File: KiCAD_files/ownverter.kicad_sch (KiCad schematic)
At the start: 10 parts, among them J101 Harting-15 and Wago 6

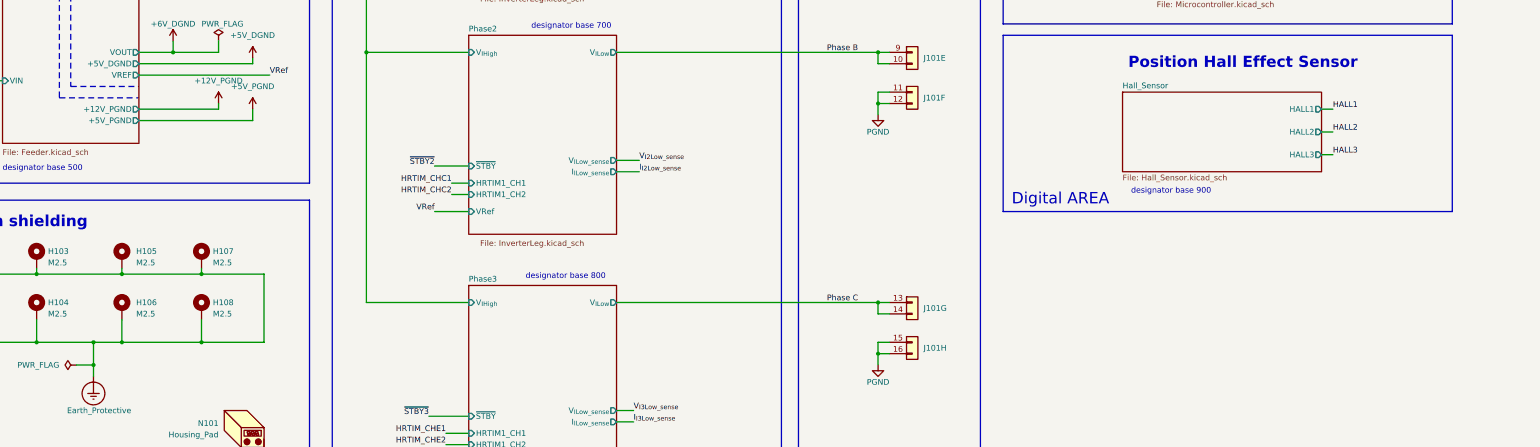
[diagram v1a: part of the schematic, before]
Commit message: better comments, especially for temp sens
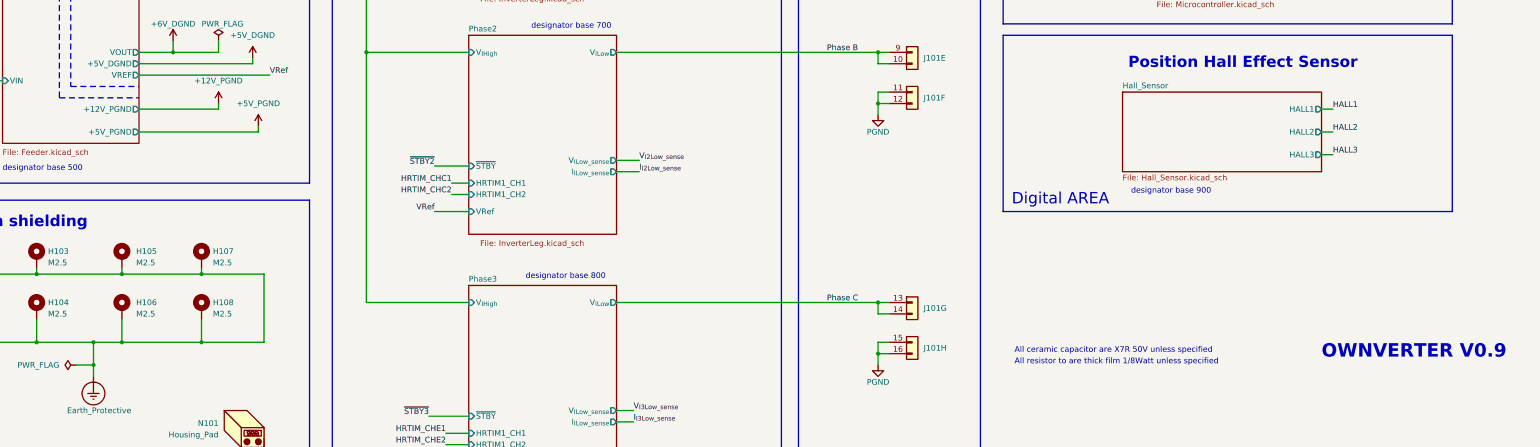
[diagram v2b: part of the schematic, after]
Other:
- note added: "All ceramic capacitor are X7R 50V unless specified"
- note added: "All resistor to are thick film 1/8Watt unless specified"
- note added: "OWNVERTER V0.9"
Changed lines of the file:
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@@
     (stroke (width 0) (type default))
   )
-  (wire (pts (xy 105.41 115.57) (xy 130.81 115.57))
+  (wire (pts (xy 105.41 118.11) (xy 132.08 118.11))
     (stroke (width 0) (type default))
   )
@@
     (stroke (width 0) (type default))
   )
-  (wire (pts (xy 130.81 113.03) (xy 130.81 115.57))
+  (wire (pts (xy 132.08 116.84) (xy 132.08 118.11))
     (stroke (width 0) (type default))
   )
@@
     (stroke (width 0) (type default))
     (fill (type none))
+  )
+  (text "All ceramic capacitor are X7R 50V unless specified"
+    (at 300.99 167.64 0)
+    (effects (font (size 1.27 1.27)) (justify left bottom))
   )
   (text "MCU\n" (at 342.9 33.02 0)
@@
   (text "Earth shielding" (at 64.77 139.7 0)
     (effects (font (face "Arial") (size 2.4892 2.4892) (thickness 0.4978) bold) (justify left bottom))
+  )
+  (text "OWNVERTER V0.9" (at 369.57 168.91 0)
+    (effects (font (size 3 3) (thickness 0.6) bold) (justify left bottom))
+  )
+  (text "All resistor to are thick film 1/8Watt unless specified"
+    (at 300.99 170.18 0)
+    (effects (font (size 1.27 1.27)) (justify left bottom))
   )
   (text "Position Hall Effect Sensor" (at 326.39 104.14 0)
@@
     )
   )
-  (symbol (lib_id "Symbols:+5V_PGND") (at 130.81 113.03 0) (unit 1)
+  (symbol (lib_id "Symbols:+5V_PGND") (at 132.08 116.84 0) (unit 1)
     (in_bom no) (on_board no) (dnp no)
-    (property "Reference" "#PWR0105" (at 132.588 113.03 90)
-      (effects (font (size 1.27 1.27)) hide)
-    )
-    (property "Value" "+5V_PGND" (at 130.81 107.95 0)
+    (property "Reference" "#PWR0105" (at 133.858 116.84 90)
+      (effects (font (size 1.27 1.27)) hide)
+    )
+    (property "Value" "+5V_PGND" (at 132.08 111.76 0)
       (effects (font (size 1.27 1.27)))
     )
-    (property "Footprint" "" (at 133.985 110.49 0)
-      (effects (font (size 1.27 1.27)) hide)
-    )
-    (property "Datasheet" "" (at 133.985 110.49 0)
+    (property "Footprint" "" (at 135.255 114.3 0)
+      (effects (font (size 1.27 1.27)) hide)
+    )
+    (property "Datasheet" "" (at 135.255 114.3 0)
       (effects (font (size 1.27 1.27)) hide)
     )
@@
       (effects (font (size 1.27 1.27)) (justify right))
     )
-    (pin "+5V_PGND" output (at 105.41 115.57 0)
-      (effects (font (size 1.27 1.27)) (justify right))
-    )
+    (pin "+5V_PGND" output (at 105.41 118.11 0)
+      (effects (font (size 1.27 1.27)) (justify right))
+    )

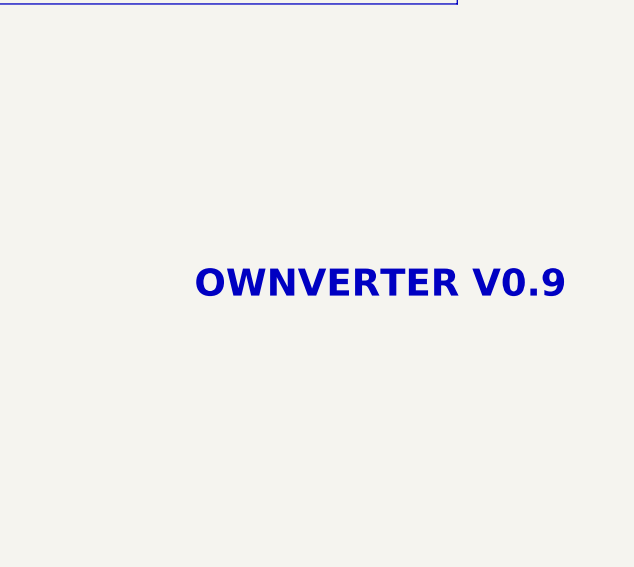
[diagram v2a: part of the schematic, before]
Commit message: Schematic freeze before PCB modifications
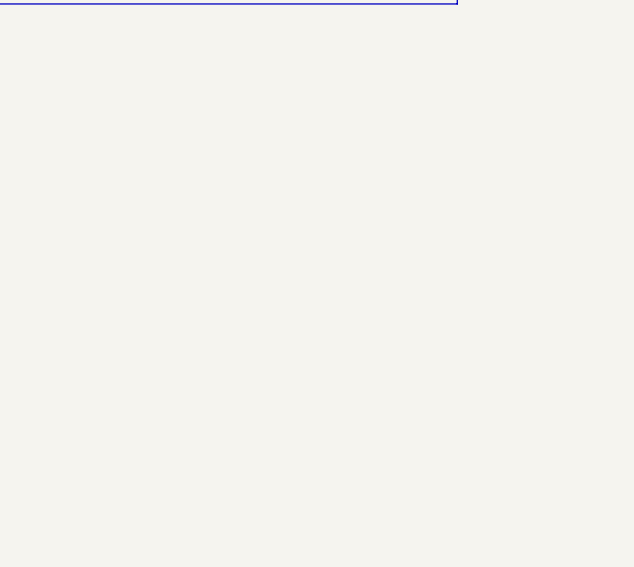
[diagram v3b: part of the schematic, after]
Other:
- note removed: "OWNVERTER V0.9"
- title: OWNVERTER V0.1 -> OWNVERTER V1.0
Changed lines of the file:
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@@
   (paper "A3")
   (title_block
-    (title "OWNVERTER V0.1")
+    (title "OWNVERTER V1.0")
     (comment 1 "TWR")
   )
@@
     (effects (font (face "Arial") (size 2.4892 2.4892) (thickness 0.4978) bold) (justify left bottom))
   )
-  (text "OWNVERTER V0.9" (at 369.57 168.91 0)
-    (effects (font (size 3 3) (thickness 0.6) bold) (justify left bottom))
-  )
   (text "All resistor to are thick film 1/8Watt unless specified"

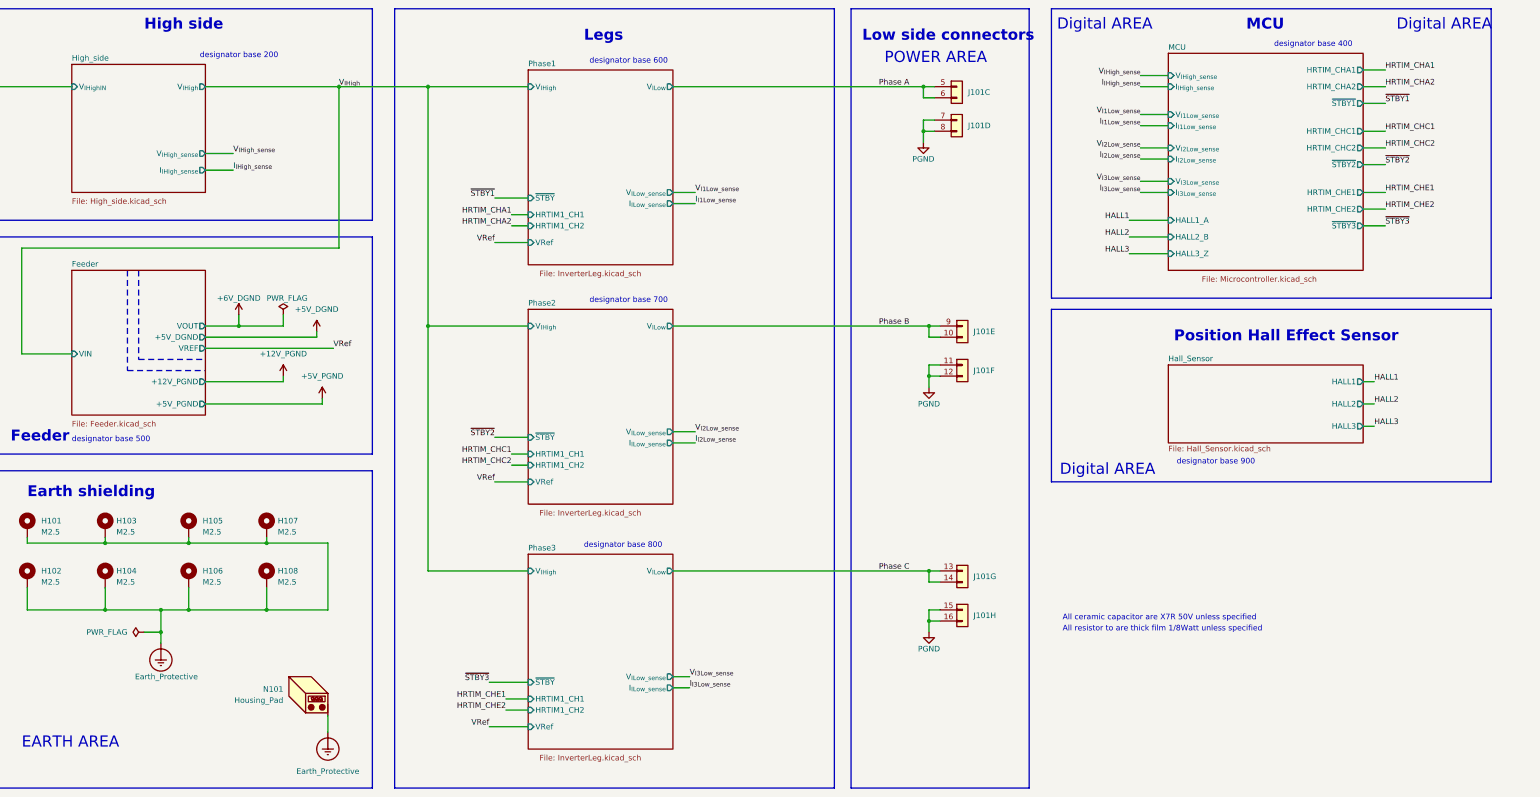
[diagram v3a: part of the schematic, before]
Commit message: changed schematic net labels for better comprehension
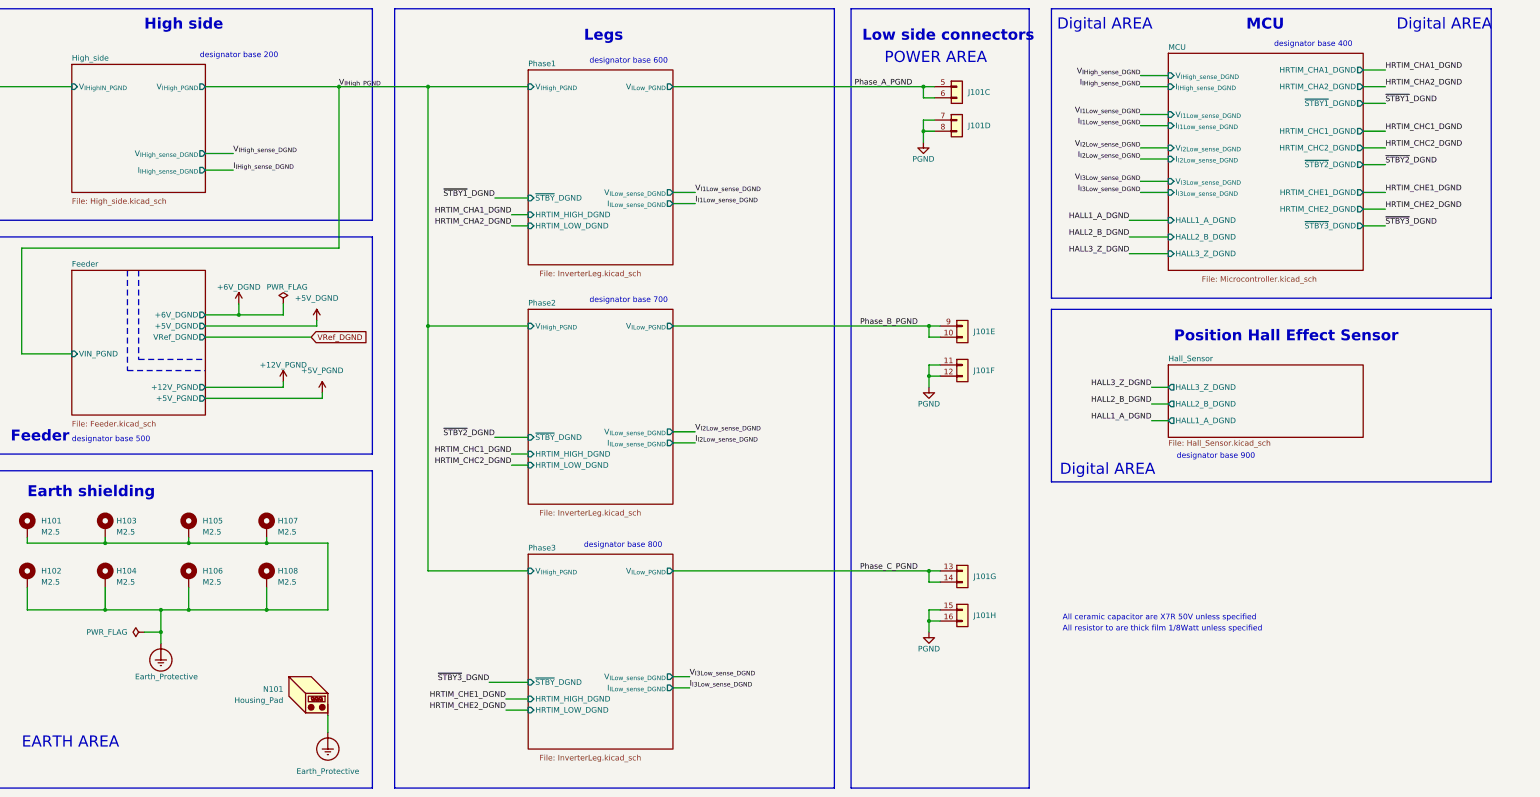
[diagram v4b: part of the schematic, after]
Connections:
- net High_side/V_{IHighIN} renamed High_side/V_{IHighIN_PGND}
- net Phase A renamed Phase_A_PGND
- net Phase B renamed Phase_B_PGND
- net Phase C renamed Phase_C_PGND
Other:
- sheet Feeder ports: added +6V_DGND, VIN_PGND, VRef_DGND; removed VIN, VOUT, VREF
- sheet Hall_Sensor ports: added HALL1_A_DGND, HALL2_B_DGND, HALL3_Z_DGND; removed HALL1, HALL2, HALL3
- sheet High_side ports: added I_{IHigh_sense_DGND}, V_{IHighIN_PGND}, V_{IHigh_PGND}, V_{IHigh_sense_DGND}; removed I_{IHigh_sense}, V_{IHighIN}, V_{IHigh_sense}, V_{IHigh}
- sheet MCU ports: added HALL1_A_DGND, HALL2_B_DGND, HALL3_Z_DGND, HRTIM_CHA1_DGND, HRTIM_CHA2_DGND, HRTIM_CHC1_DGND, HRTIM_CHC2_DGND, HRTIM_CHE1_DGND, HRTIM_CHE2_DGND, I_{I1Low_sense_DGND}, I_{I2Low_sense_DGND}, I_{I3Low_sense_DGND}, I_{IHigh_sense_DGND}, V_{I1Low_sense_DGND}, V_{I2Low_sense_DGND}, V_{I3Low_sense_DGND}, V_{IHigh_sense_DGND}, ~{STBY1}_DGND, ~{STBY2}_DGND, ~{STBY3}_DGND; removed HALL1_A, HALL2_B, HALL3_Z, HRTIM_CHA1, HRTIM_CHA2, HRTIM_CHC1, HRTIM_CHC2, HRTIM_CHE1, HRTIM_CHE2, I_{I1Low_sense}, I_{I2Low_sense}, I_{I3Low_sense}, I_{IHigh_sense}, V_{I1Low_sense}, V_{I2Low_sense}, V_{I3Low_sense}, V_{IHigh_sense}, ~{STBY1}, ~{STBY2}, ~{STBY3}
- sheet Phase1 ports: added HRTIM_HIGH_DGND, HRTIM_LOW_DGND, I_{ILow_sense_DGND}, V_{IHigh_PGND}, V_{ILow_PGND}, V_{ILow_sense_DGND}, ~{STBY}_DGND; removed HRTIM1_CH1, HRTIM1_CH2, I_{ILow_sense}, VRef, V_{IHigh}, V_{ILow_sense}, V_{ILow}, ~{STBY}
- sheet Phase2 ports: added HRTIM_HIGH_DGND, HRTIM_LOW_DGND, I_{ILow_sense_DGND}, V_{IHigh_PGND}, V_{ILow_PGND}, V_{ILow_sense_DGND}, ~{STBY}_DGND; removed HRTIM1_CH1, HRTIM1_CH2, I_{ILow_sense}, VRef, V_{IHigh}, V_{ILow_sense}, V_{ILow}, ~{STBY}
- sheet Phase3 ports: added HRTIM_HIGH_DGND, HRTIM_LOW_DGND, I_{ILow_sense_DGND}, V_{IHigh_PGND}, V_{ILow_PGND}, V_{ILow_sense_DGND}, ~{STBY}_DGND; removed HRTIM1_CH1, HRTIM1_CH2, I_{ILow_sense}, VRef, V_{IHigh}, V_{ILow_sense}, V_{ILow}, ~{STBY}

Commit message: wip
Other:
- note removed: "Digital AREA"
- note removed: "POWER AREA"
- title: OWNVERTER V1.0 -> OWNVERTER V1.1
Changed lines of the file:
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@@
   (paper "A3")
   (title_block
-    (title "OWNVERTER V1.0")
+    (title "OWNVERTER V1.1")
     (comment 1 "TWR")
   )
@@
   )
   (text "MCU\n" (at 342.9 33.02 0)
-    (effects (font (face "Arial") (size 2.4892 2.4892) (thickness 0.4978) bold) (justify left bottom))
-  )
-  (text "Digital AREA\n" (at 300.355 134.62 0)
-    (effects (font (face "Arial") (size 2.54 2.54)) (justify left bottom))
+    (effects (font (face "Arial") (size 2.54 2.54) (thickness 0.4978) bold) (justify left bottom))
   )
   (text "High side\n" (at 91.44 33.02 0)
-    (effects (font (face "Arial") (size 2.4892 2.4892) (thickness 0.4978) bold) (justify left bottom))
+    (effects (font (face "Arial") (size 2.54 2.54) (thickness 0.4978) bold) (justify left bottom))
   )
   (text "designator base 600" (at 193.04 40.64 0)
@@
     (effects (font (size 1.27 1.27)) (justify left bottom))
   )
-  (text "Legs" (at 191.77 35.56 0)
-    (effects (font (face "Arial") (size 2.4892 2.4892) (thickness 0.4978) bold) (justify left bottom))
+  (text "Legs" (at 191.77 33.02 0)
+    (effects (font (face "Arial") (size 2.54 2.54) (thickness 0.4978) bold) (justify left bottom))
   )
   (text "EARTH AREA\n" (at 63.5 196.85 0)
@@
   )
   (text "Feeder" (at 60.96 127 0)
-    (effects (font (face "Arial") (size 2.4892 2.4892) (thickness 0.4978) bold) (justify left bottom))
+    (effects (font (face "Arial") (size 2.54 2.54) (thickness 0.4978) bold) (justify left bottom))
   )
   (text "designator base 800" (at 191.77 151.13 0)
     (effects (font (size 1.27 1.27)) (justify left bottom))
   )
-  (text "POWER AREA\n" (at 260.35 40.64 0)
-    (effects (font (face "Arial") (size 2.54 2.54)) (justify left bottom))
-  )
   (text "designator base 200" (at 104.14 39.37 0)
     (effects (font (size 1.27 1.27)) (justify left bottom))
   )
   (text "Earth shielding" (at 64.77 139.7 0)
-    (effects (font (face "Arial") (size 2.4892 2.4892) (thickness 0.4978) bold) (justify left bottom))
+    (effects (font (face "Arial") (size 2.54 2.54) (thickness 0.4978) bold) (justify left bottom))
   )
   (text "All resistor to are thick film 1/8Watt unless specified"
@@
     (effects (font (size 1.27 1.27)) (justify left bottom))
   )
-  (text "Position Hall Effect Sensor" (at 326.39 104.14 0)
-    (effects (font (face "Arial") (size 2.4892 2.4892) (thickness 0.4978) bold) (justify left bottom))
+  (text "Position Hall Effect Sensor" (at 325.12 102.87 0)
+    (effects (font (face "Arial") (size 2.54 2.54) (thickness 0.4978) bold) (justify left bottom))
   )
   (text "designator base 400" (at 349.25 36.83 0)
@@
   )
   (text "High side connectors" (at 17.78 34.29 0)
-    (effects (font (face "Arial") (size 2.4892 2.4892) (thickness 0.4978) bold) (justify left bottom))
-  )
-  (text "Digital AREA\n" (at 377.19 33.02 0)
-    (effects (font (face "Arial") (size 2.54 2.54)) (justify left bottom))
-  )
-  (text "POWER AREA\n" (at 22.86 39.37 0)
-    (effects (font (face "Arial") (size 2.54 2.54)) (justify left bottom))
+    (effects (font (face "Arial") (size 2.54 2.54) (thickness 0.4978) bold) (justify left bottom))
   )
   (text "designator base 500" (at 74.93 127 0)
     (effects (font (size 1.27 1.27)) (justify left bottom))
   )
-  (text "Digital AREA\n" (at 299.72 33.02 0)
-    (effects (font (face "Arial") (size 2.54 2.54)) (justify left bottom))
-  )
   (text "Low side connectors" (at 255.27 35.56 0)
-    (effects (font (face "Arial") (size 2.4892 2.4892) (thickness 0.4978) bold) (justify left bottom))
+    (effects (font (face "Arial") (size 2.54 2.54) (thickness 0.4978) bold) (justify left bottom))
   )
   (label "HALL3_Z_DGND" (at 321.31 114.3 180) (fields_autoplaced)

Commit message: wip
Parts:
- added J?: Harting-15 and Wago 6, Footprints:Harting - 15contacts and Wago, symbol Symbols:Harting 15 contacts and WAGO
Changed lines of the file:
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@@
+    )
+  )
+  (symbol (lib_id "Symbols:Harting 15 contacts and WAGO") (at 279.4 184.15 0) (unit 8)
+    (in_bom yes) (on_board yes) (dnp no) (fields_autoplaced)
+    (property "Reference" "J?" (at 281.94 185.42 0)
+      (effects (font (size 1.27 1.27)) (justify left))
+    )
+    (property "Value" "Harting-15 and Wago 6" (at 278.13 189.23 0)
+      (effects (font (size 1.27 1.27)) hide)
+    )
+    (property "Footprint" "Footprints:Harting - 15contacts and Wago" (at 278.13 179.07 0)
+      (effects (font (size 1.27 1.27)) hide)
+    )
+    (property "Datasheet" "~" (at 279.4 184.15 0)
+      (effects (font (size 1.27 1.27)) hide)
+    )
+    (property "manf#" "2604-1108" (at 279.4 184.15 0)
+      (effects (font (size 1.27 1.27)) hide)
+    )
+    (pin "1")
+    (pin "2")
+    (pin "3")
+    (pin "4")
+    (pin "5")
+    (pin "6")
+    (pin "7")
+    (pin "8")
+    (pin "10")
+    (pin "9")
+    (pin "11")
+    (pin "12")
+    (pin "13")
+    (pin "14")
+    (pin "15")
+    (pin "16")
+    (instances
+      (project "ownverter"
+        (path "/8d0c1d66-35ef-4a53-a28f-436a11b54f42"
+          (reference "J?") (unit 8)
+        )
+      )
     )
   )
